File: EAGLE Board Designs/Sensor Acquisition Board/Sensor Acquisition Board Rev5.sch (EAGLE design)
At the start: 163 parts, among them J1 CONNECTOR-8_μF_S_RA_, J10 CONNECTOR-10_MF_T_V_, J11 CONNECTOR-2_MICROFIT_SMD_RIGH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, J12 CONNECTOR-6_μF_T_V_BLACK, J13 CONNECTOR-4_μF_T_V_BLACK, J14 CONNECTOR-8_μF_S_RA_, J15 CONNECTOR-4_μF_T_V_BLACK, J16 CONNECTOR-8_μF_S_RA_, J2 CONNECTOR-4_μF_S_RA_, J3 CONNECTOR-4_μF_S_RA_, J4 CONNECTOR-4_μF_S_RA_, J5 CONNECTOR-4_μF_S_RA_, J6 CONNECTOR-8_μF_S_RA_, J7 CONNECTOR-4_μF_S_RA_, J8 CONNECTOR-2_MICROFIT_SMD_RIGH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, J9 CONNECTOR-4_μF_S_RA_, T1 78613/3C_78613/3C, T2 78613/3C_78613/3C, U1 VOLTAGE_REGULATOR_SOT-223_3.3V, U10 MAX3227, U11 LTC6820, U12 LTC6820, U13 TCAN1051HQV-Q1, U14 MAX3075, U15 MCP3208, U2 MAX7404, U3 MAX7404, U4 MAX7404, U5 MAX7404, U6 MAX7404, U7 MAX7404, U8 MAX7404, U9 MAX7404

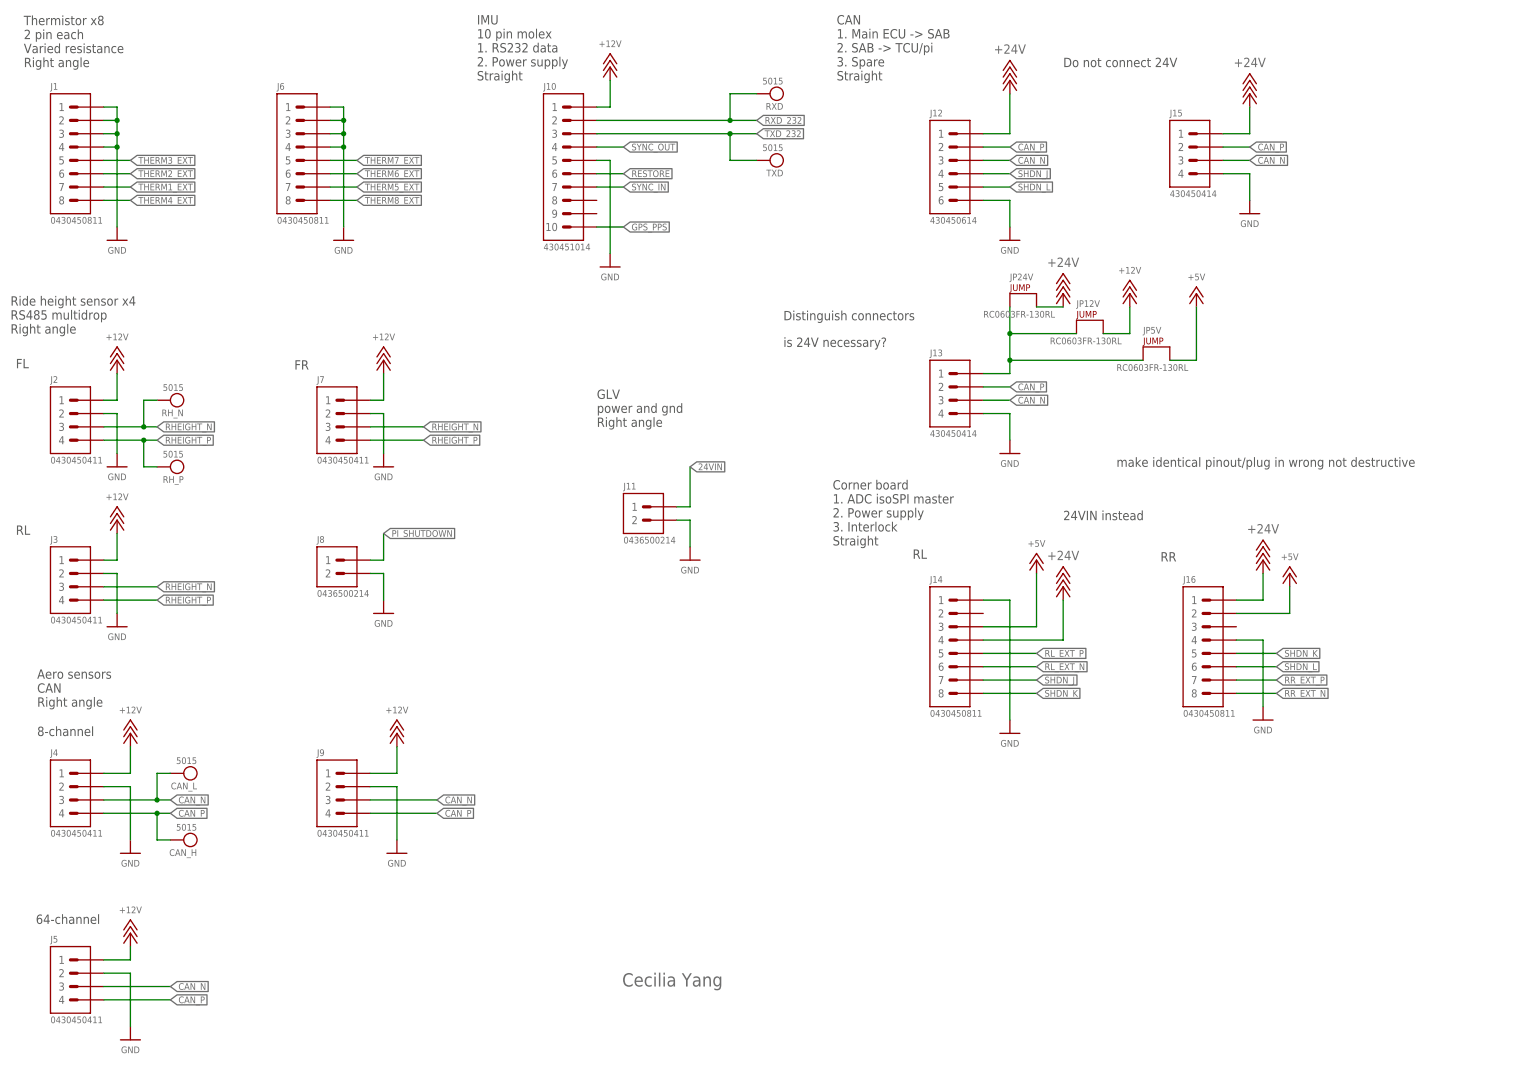
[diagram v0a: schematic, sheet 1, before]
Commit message: change connectors
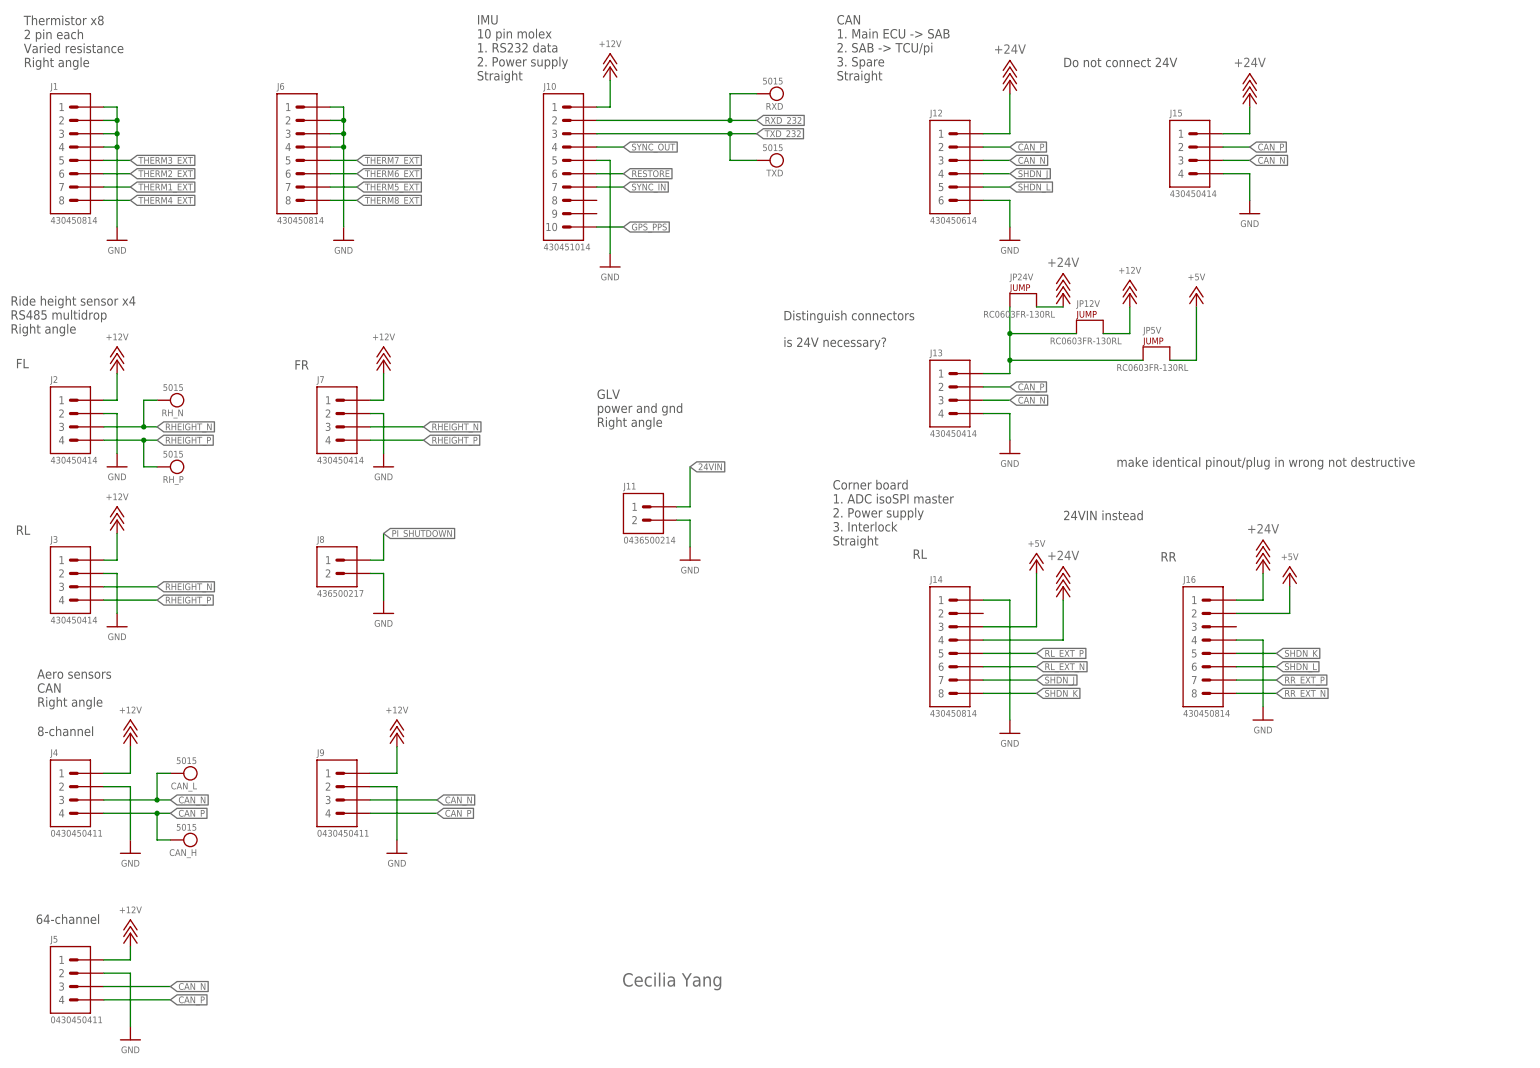
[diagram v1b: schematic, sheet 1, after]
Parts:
- J1, J14, J16, J6: value CONNECTOR-8_μF_S_RA_ -> CONNECTOR-8_μF_T_V_BLACK; device HyTechDevices:CONNECTOR-8_μF_S_RA_ -> HyTechDevices:CONNECTOR-8_μF_T_V_BLACK
- J2, J3, J7: value CONNECTOR-4_μF_S_RA_ -> CONNECTOR-4_μF_T_V_BLACK; device HyTechDevices:CONNECTOR-4_μF_S_RA_ -> HyTechDevices:CONNECTOR-4_μF_T_V_BLACK
- J8: value CONNECTOR-2_MICROFIT_SMD_RIGHTANGLE_02_SINGLE_BLACK -> CONNECTOR-2_μF_T_V_BLACK; device HyTechDevices:CONNECTOR-2_MICROFIT_SMD_RIGHTANGLE_02_SINGLE_BLACK -> HyTechDevices:CONNECTOR-2_μF_T_V_BLACK
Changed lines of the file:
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@@
 <parts>
 <part name="FRAME1" library="HyTechFrames" deviceset="FRAME" device=""/>
-<part name="J2" library="HyTechDevices" deviceset="CONNECTOR-4_?_*" device="μF_S_RA"/>
-<part name="J7" library="HyTechDevices" deviceset="CONNECTOR-4_?_*" device="μF_S_RA"/>
-<part name="J3" library="HyTechDevices" deviceset="CONNECTOR-4_?_*" device="μF_S_RA"/>
+<part name="J2" library="HyTechDevices" deviceset="CONNECTOR-4_?_*" device="μF_T_V" technology="BLACK" value="CONNECTOR-4_μF_T_V_BLACK"/>
+<part name="J7" library="HyTechDevices" deviceset="CONNECTOR-4_?_*" device="μF_T_V" technology="BLACK" value="CONNECTOR-4_μF_T_V_BLACK"/>
+<part name="J3" library="HyTechDevices" deviceset="CONNECTOR-4_?_*" device="μF_T_V" technology="BLACK" value="CONNECTOR-4_μF_T_V_BLACK"/>
 <part name="J4" library="HyTechDevices" deviceset="CONNECTOR-4_?_*" device="μF_S_RA" value="CONNECTOR-4_μF_S_RA_"/>
 <part name="J9" library="HyTechDevices" deviceset="CONNECTOR-4_?_*" device="μF_S_RA" value="CONNECTOR-4_μF_S_RA_"/>
@@
 <part name="JP12V" library="HyTechDevices" deviceset="JUMPER_?_*" device="0603" value="JUMPER_0603_"/>
 <part name="JP5V" library="HyTechDevices" deviceset="JUMPER_?_*" device="0603" value="JUMPER_0603_"/>
-<part name="J14" library="HyTechDevices" deviceset="CONNECTOR-8_?_*" device="μF_S_RA" value="CONNECTOR-8_μF_S_RA_"/>
-<part name="J16" library="HyTechDevices" deviceset="CONNECTOR-8_?_*" device="μF_S_RA" value="CONNECTOR-8_μF_S_RA_"/>
+<part name="J14" library="HyTechDevices" deviceset="CONNECTOR-8_?_*" device="μF_T_V" technology="BLACK" value="CONNECTOR-8_μF_T_V_BLACK"/>
+<part name="J16" library="HyTechDevices" deviceset="CONNECTOR-8_?_*" device="μF_T_V" technology="BLACK" value="CONNECTOR-8_μF_T_V_BLACK"/>
 <part name="P28" library="HyTechSupplies" deviceset="+24V" device=""/>
 <part name="P92" library="HyTechSupplies" deviceset="+24V" device=""/>
@@
 <part name="C41" library="HyTechDevices" deviceset="CAPACITOR_?_*" device="0603" technology="10V_1UF"/>
 <part name="P147" library="HyTechSupplies" deviceset="GND" device=""/>
-<part name="J1" library="HyTechDevices" deviceset="CONNECTOR-8_?_*" device="μF_S_RA"/>
-<part name="J6" library="HyTechDevices" deviceset="CONNECTOR-8_?_*" device="μF_S_RA"/>
+<part name="J1" library="HyTechDevices" deviceset="CONNECTOR-8_?_*" device="μF_T_V" technology="BLACK" value="CONNECTOR-8_μF_T_V_BLACK"/>
+<part name="J6" library="HyTechDevices" deviceset="CONNECTOR-8_?_*" device="μF_T_V" technology="BLACK" value="CONNECTOR-8_μF_T_V_BLACK"/>
 <part name="R8" library="HyTechDevices" deviceset="RESISTOR_?_*" device="0603" technology="8.35K"/>
 <part name="R9" library="HyTechDevices" deviceset="RESISTOR_?_*" device="0603" technology="8.35K"/>
@@
 <part name="P16" library="HyTechSupplies" deviceset="GND" device=""/>
 <part name="P54" library="HyTechSupplies" deviceset="+3V3" device=""/>
-<part name="J8" library="HyTechDevices" deviceset="CONNECTOR-2_?_*" device="MICROFIT_SMD_RIGHTANGLE_02_SINGLE" technology="BLACK"/>
+<part name="J8" library="HyTechDevices" deviceset="CONNECTOR-2_?_*" device="μF_T_V" technology="BLACK" value="CONNECTOR-2_μF_T_V_BLACK"/>
 <part name="P109" library="HyTechSupplies" deviceset="GND" device=""/>
 </parts>

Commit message: thermistor cap notes
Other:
- note added: "1uF 0603 caps"
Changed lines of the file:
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@@
 <text x="114.3" y="139.7" size="1.778" layer="97">get rid of max's
 switch to passives</text>
+<text x="101.6" y="193.04" size="1.778" layer="97">1uF 0603 caps</text>
 </plain>
 <instances>

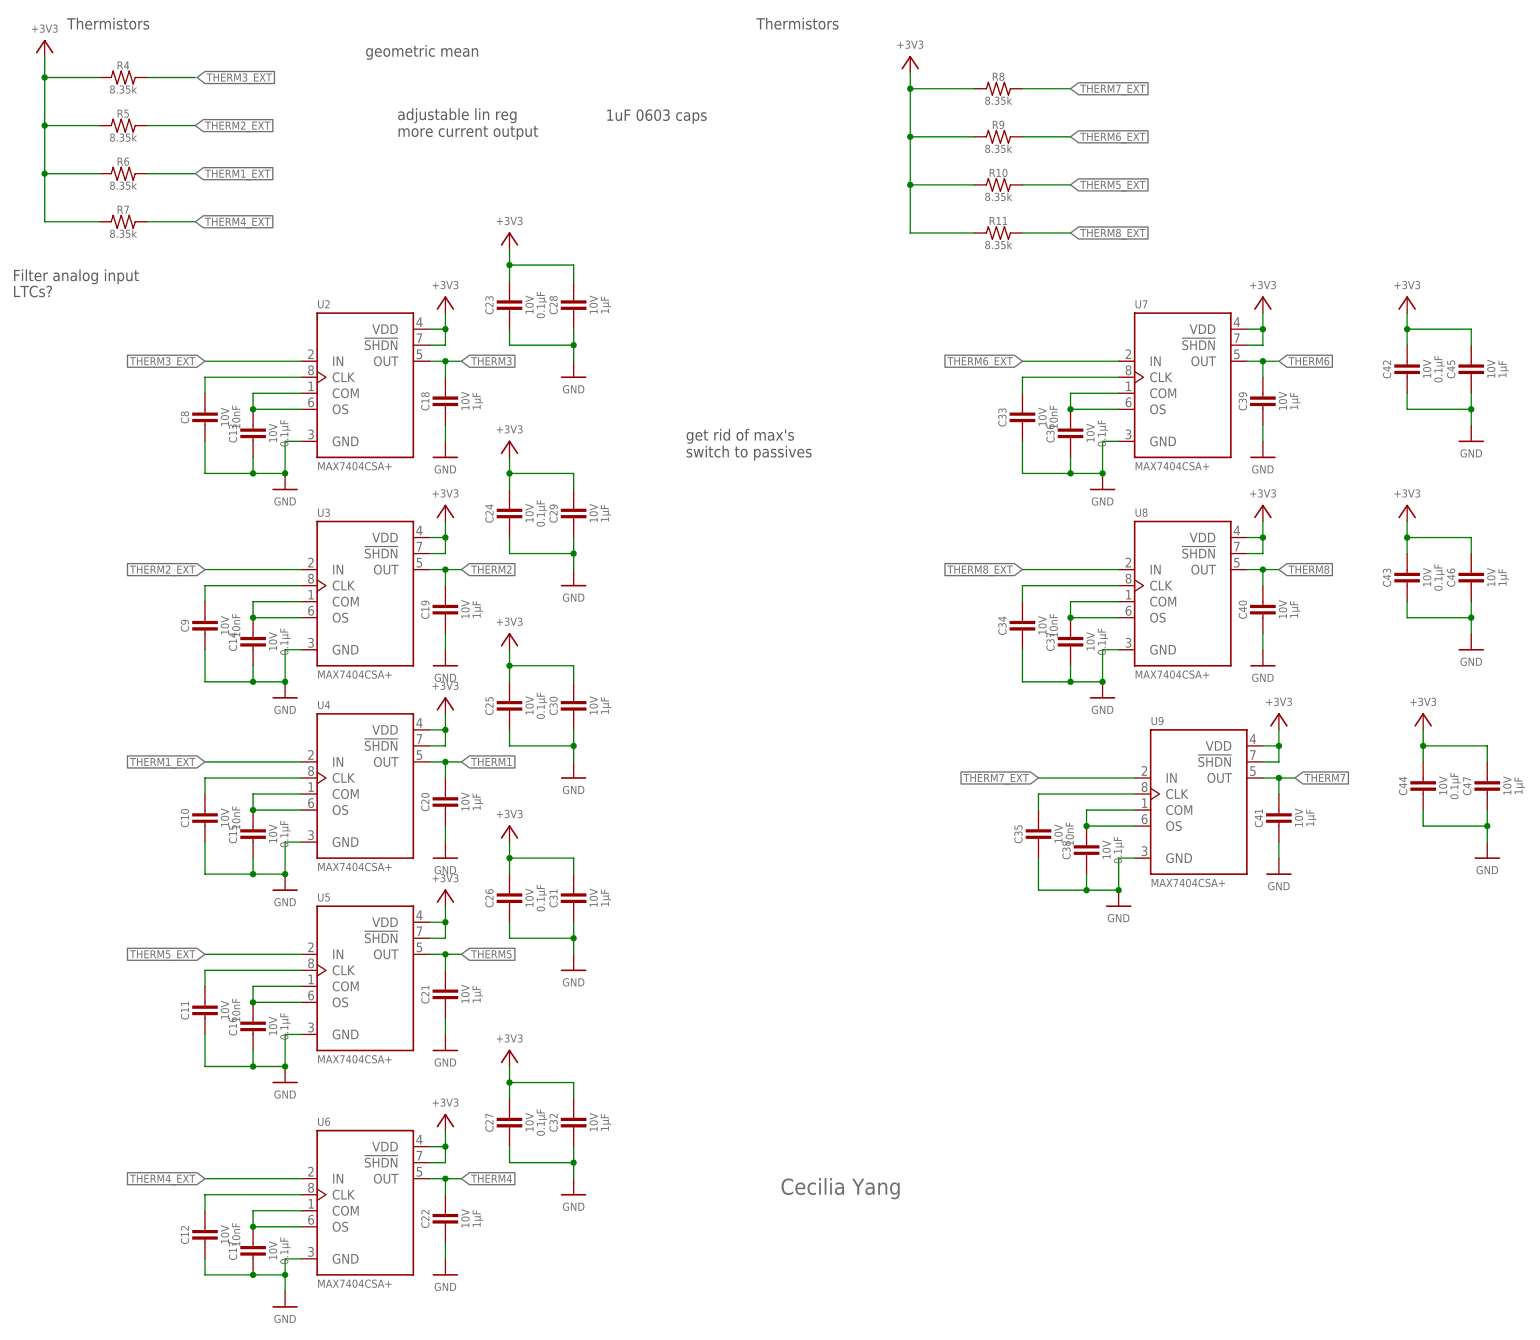
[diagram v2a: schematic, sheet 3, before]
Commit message: swap max's for 1uF cap
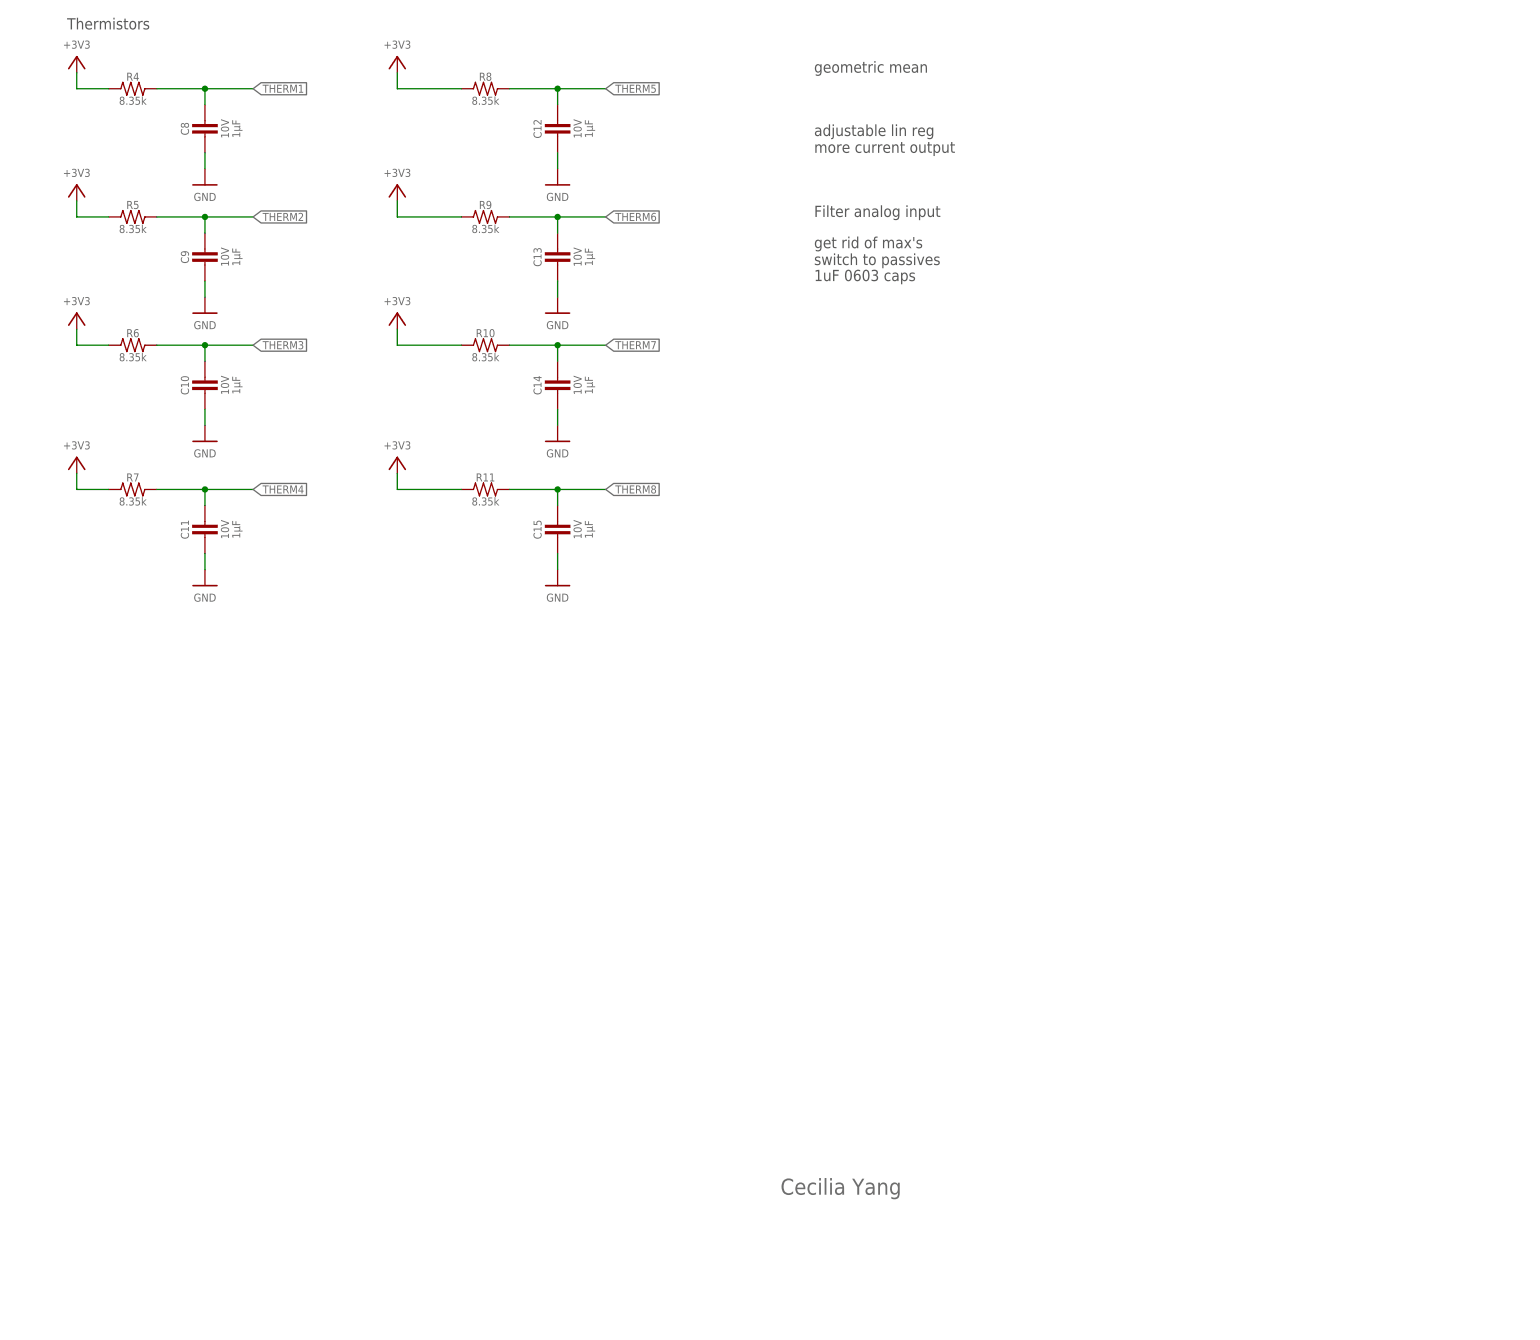
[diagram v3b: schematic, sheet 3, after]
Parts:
- removed C16, C17, C23, C24, C25, C26, C27, C36, C37, C38, C42, C43, C44: CAPACITOR_0603_10V_0.1UF, HyTechDevices:CAPACITOR_0603_10V_0.1UF
- removed C18, C19, C20, C21, C22, C28, C29, C30, C31, C32, C39, C40, C41, C45, C46, C47: CAPACITOR_0603_10V_1UF, HyTechDevices:CAPACITOR_0603_10V_1UF
- removed C33, C34, C35: CAPACITOR_0603_10V_10NF, HyTechDevices:CAPACITOR_0603_10V_10NF
- removed U2, U3, U4, U5, U6, U7, U8, U9: MAX7404, HyTechDevices:MAX7404
- C10, C11, C12, C8, C9: value CAPACITOR_0603_10V_10NF -> CAPACITOR_0603_10V_1UF; device HyTechDevices:CAPACITOR_0603_10V_10NF -> HyTechDevices:CAPACITOR_0603_10V_1UF
- C13, C14, C15: value CAPACITOR_0603_10V_0.1UF -> CAPACITOR_0603_10V_1UF; device HyTechDevices:CAPACITOR_0603_10V_0.1UF -> HyTechDevices:CAPACITOR_0603_10V_1UF
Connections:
- removed net N$10: C11.1, U5.CLK
- removed net N$11: C10.1, U4.CLK
- removed net N$12: C15.1, U4.COM, U4.OS
- removed net N$13: C16.1, U5.COM, U5.OS
- removed net N$14: C12.1, U6.CLK
- removed net N$15: C17.1, U6.COM, U6.OS
- removed net N$33: C33.1, U7.CLK
- removed net N$34: C36.1, U7.COM, U7.OS
- removed net N$35: C34.1, U8.CLK
- removed net N$36: C37.1, U8.COM, U8.OS
- removed net N$37: C35.1, U9.CLK
- removed net N$38: C38.1, U9.COM, U9.OS
- removed net N$6: C8.1, U2.CLK
- removed net N$7: C13.1, U2.COM, U2.OS
- removed net N$8: C9.1, U3.CLK
- removed net N$9: C14.1, U3.COM, U3.OS
- removed net THERM1_EXT: J1.7, R6.2, U4.IN
- removed net THERM2_EXT: J1.6, R5.2, U3.IN
- removed net THERM3_EXT: J1.5, R4.2, U2.IN
- removed net THERM4_EXT: J1.8, R7.2, U6.IN
- removed net THERM5_EXT: J6.7, R10.2, U5.IN
- removed net THERM6_EXT: J6.6, R9.2, U7.IN
- removed net THERM7_EXT: J6.5, R8.2, U9.IN
- removed net THERM8_EXT: J6.8, R11.2, U8.IN
- net +3V3: no longer C23.1, C24.1, C25.1, C26.1, C27.1, C28.1, C29.1, C30.1, C31.1, C32.1, C42.1, C43.1, C44.1, C45.1, C46.1, C47.1, U2.!SHDN, U2.VDD, U3.!SHDN, U3.VDD, U4.!SHDN, U4.VDD, U5.!SHDN, U5.VDD, U6.!SHDN, U6.VDD, U7.!SHDN, U7.VDD, U8.!SHDN, U8.VDD, U9.!SHDN, U9.VDD
- net GND: no longer C16.2, C17.2, C18.2, C19.2, C20.2, C21.2, C22.2, C23.2, C24.2, C25.2, C26.2, C27.2, C28.2, C29.2, C30.2, C31.2, C32.2, C33.2, C34.2, C35.2, C36.2, C37.2, C38.2, C39.2, C40.2, C41.2, C42.2, C43.2, C44.2, C45.2, C46.2, C47.2, U2.GND, U3.GND, U4.GND, U5.GND, U6.GND, U7.GND, U8.GND, U9.GND
- net THERM1: now also C8.1, J1.7, R4.2; no longer C20.1, U4.OUT
- net THERM2: now also C9.1, J1.6, R5.2; no longer C19.1, U3.OUT
- net THERM3: now also C10.1, J1.5, R6.2; no longer C18.1, U2.OUT
- net THERM4: now also C11.1, J1.8, R7.2; no longer C22.1, U6.OUT
- net THERM5: now also C12.1, J6.7, R8.2; no longer C21.1, U5.OUT
- net THERM6: now also C13.1, J6.6, R9.2; no longer C39.1, U7.OUT
- net THERM7: now also C14.1, J6.5, R10.2; no longer C41.1, U9.OUT
- net THERM8: now also C15.1, J6.8, R11.2; no longer C40.1, U8.OUT
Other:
- note removed: "LTCs?"
- moved on the sheet: C10, C11, C12, C13, C14, C15, C8, C9, R10, R11, R4, R5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
